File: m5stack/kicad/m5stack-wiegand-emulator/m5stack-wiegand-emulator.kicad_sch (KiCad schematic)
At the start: 26 parts, among them J1 2x15 socket header, J2 2x15 pin header, J3 1x5 female, U1 RP2040, U2 6N135S, U3 6N135S, U4 6N135S, U5 SN74AHCT125N

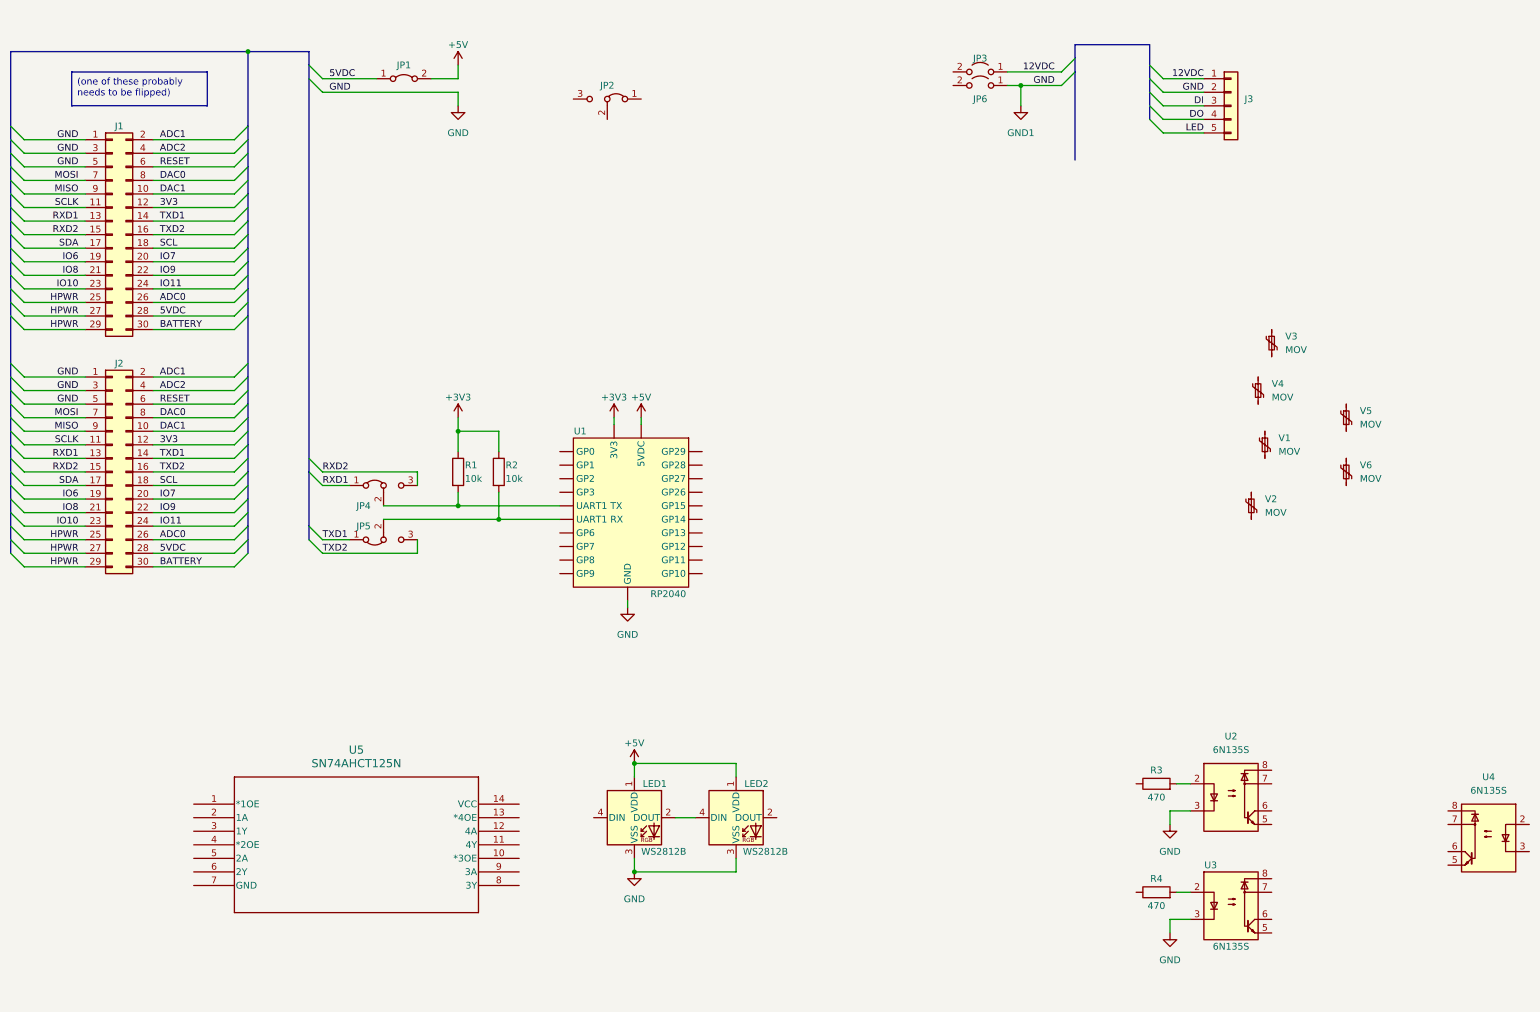
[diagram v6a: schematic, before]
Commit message: M5Stack: reworked WS2821 to use SN74HCT1G125
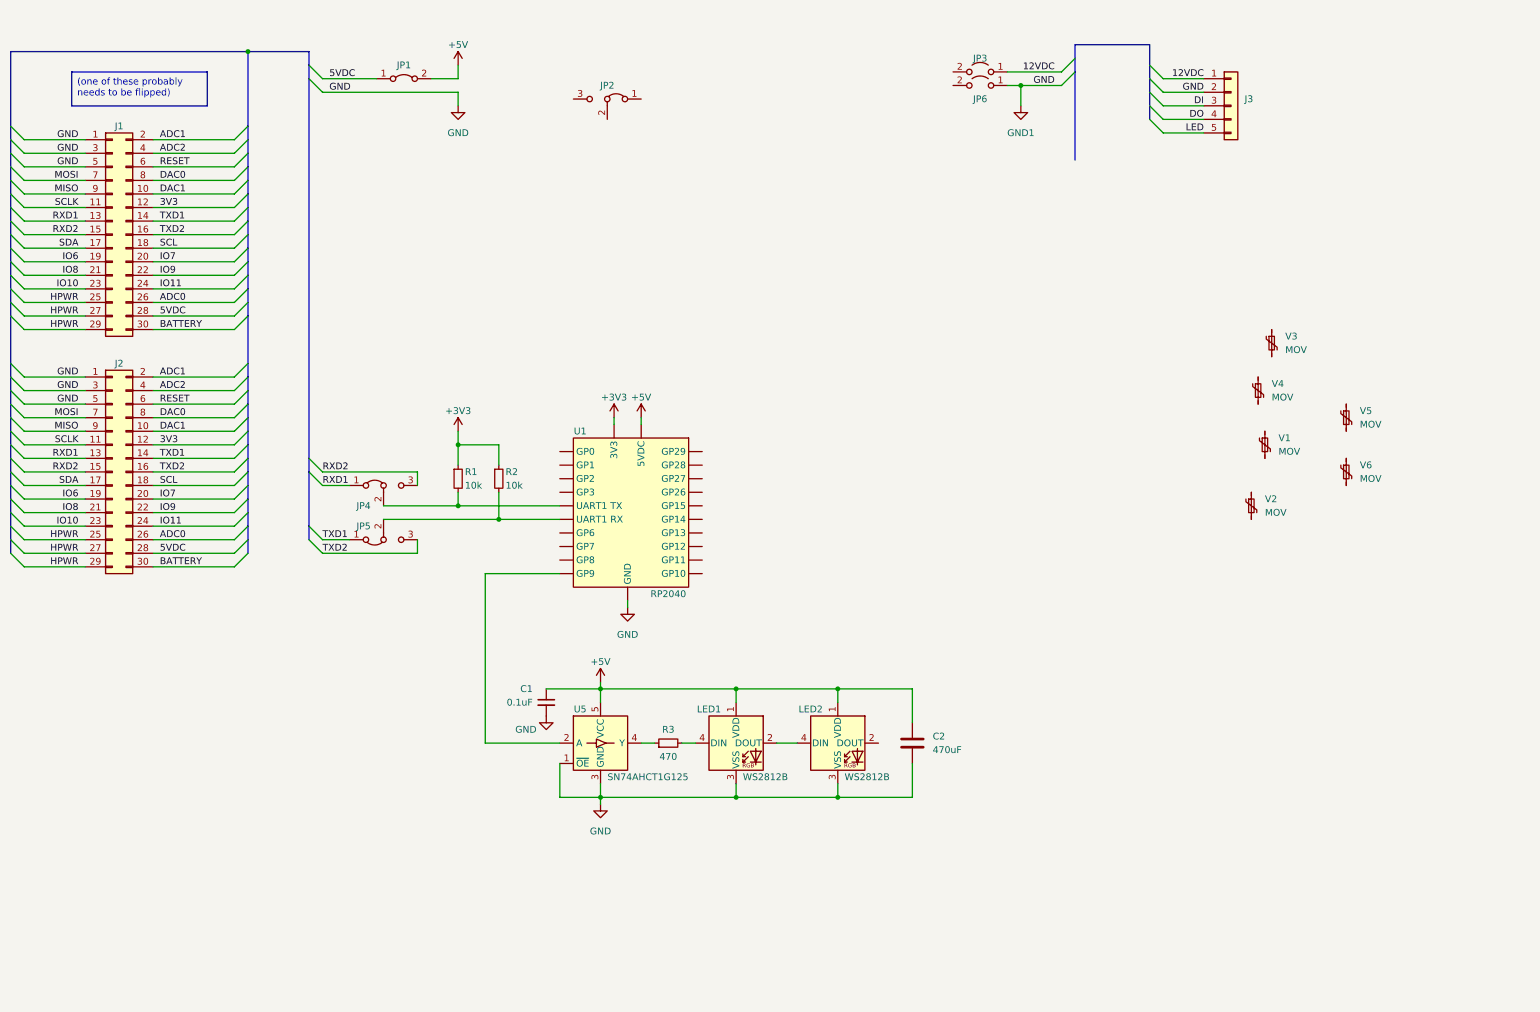
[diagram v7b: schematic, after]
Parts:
- removed R3, R4: 470, symbol Device:R
- removed U2, U3, U4: 6N135S, Package_DIP:SMDIP-8_W9.53mm, symbol Isolator:6N135S
- removed U5: SN74AHCT125N, N14, symbol uhppoted:SN74AHCT125N
- added C1: 0.1uF, symbol Device:C_Small
- added C2: 470uF, symbol Device:C
- added R3: 470, symbol Device:R_Small
- added U5: SN74AHCT1G125, Package_TO_SOT_SMD:SOT-23-5, symbol uhppoted:SN74AHCT1G125
- R1, R2: symbol Device:R -> Device:R_Small
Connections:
- net +5V: now also C1.1, C2.1, U5.5 (VCC)
- net GND: now also C1.2, C2.2, U5.1 (~{OE}), U5.3 (GND)
- net at LED1.4 (DIN): now also R3.2
- net at U1.14 (GP9): now also U5.2 (A)
- new net: R3.1, U5.4 (Y)
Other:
- moved on the sheet: LED1, LED2, R1, R2

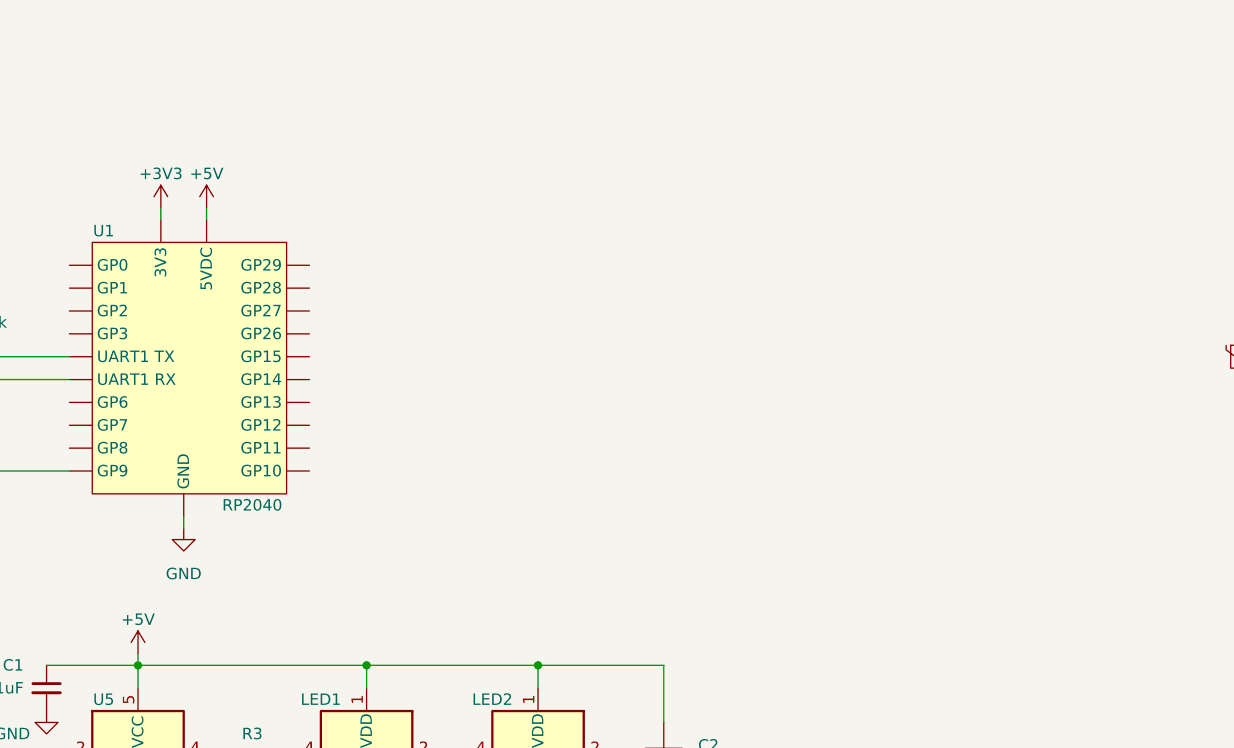
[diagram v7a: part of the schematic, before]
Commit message: M5: ISOW7842 digital isolator and SN74LVC2G12 line driver
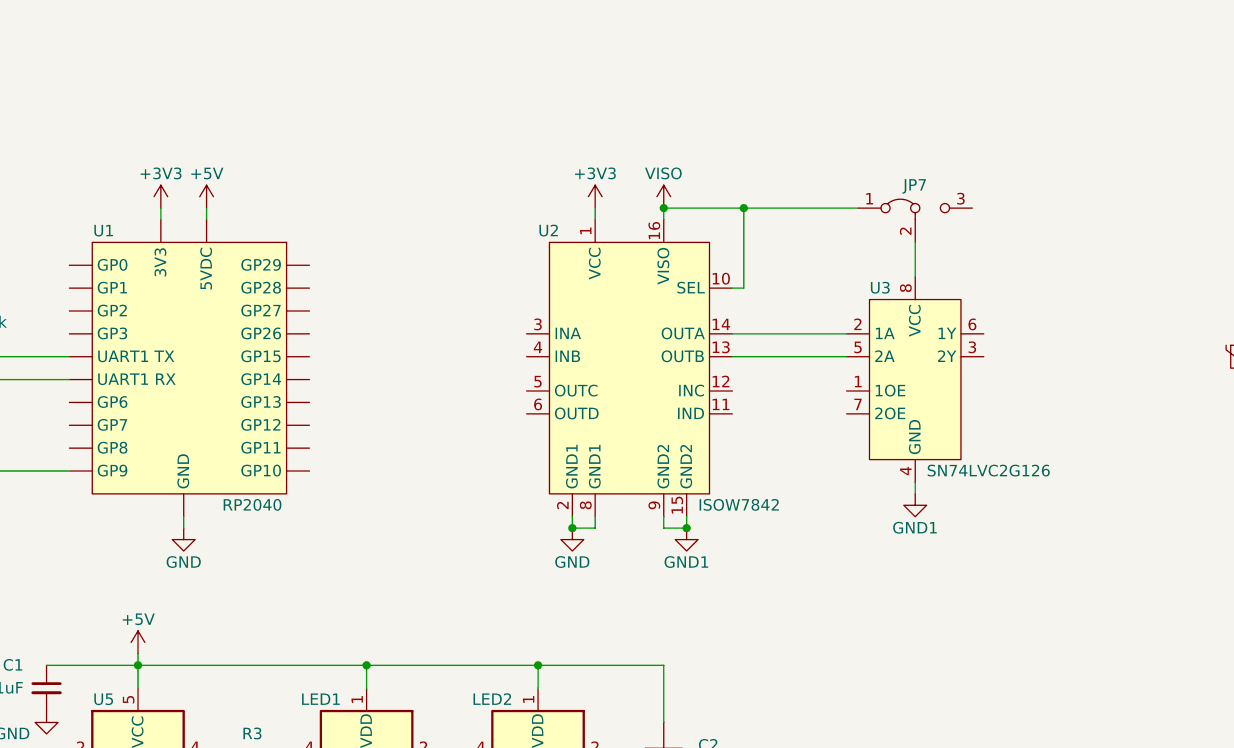
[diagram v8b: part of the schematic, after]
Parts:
- added JP7: Jumper_3_Bridged12, symbol Jumper:Jumper_3_Bridged12
- added U2: ISOW7842, Package_SO:SOIC-16W_7.5x12.8mm_P1.27mm, symbol uhppoted:ISOW7842
- added U3: SN74LVC2G126, Package_SO:VSSOP-8_2.4x2.1mm_P0.5mm, symbol uhppoted:SN74LVC2G126
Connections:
- net +3V3: now also U2.1 (VCC)
- net GND: now also U2.15 (GND2), U2.2 (GND1), U2.8 (GND1), U2.9 (GND2), U3.4 (GND)
- new net: U2.13 (OUTB), U3.5 (2A)
- new net: U2.14 (OUTA), U3.2 (1A)
- new net: JP7.2 (C), U3.8 (VCC)
- new net VISO: JP7.1 (A), U2.10 (SEL), U2.16 (VISO)
